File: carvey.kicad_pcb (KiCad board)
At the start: 2 copper layers, 48.2 x 14.7 mm, 6 parts, among them J1 Conn_01x04, SW1 SW_Push_Dual

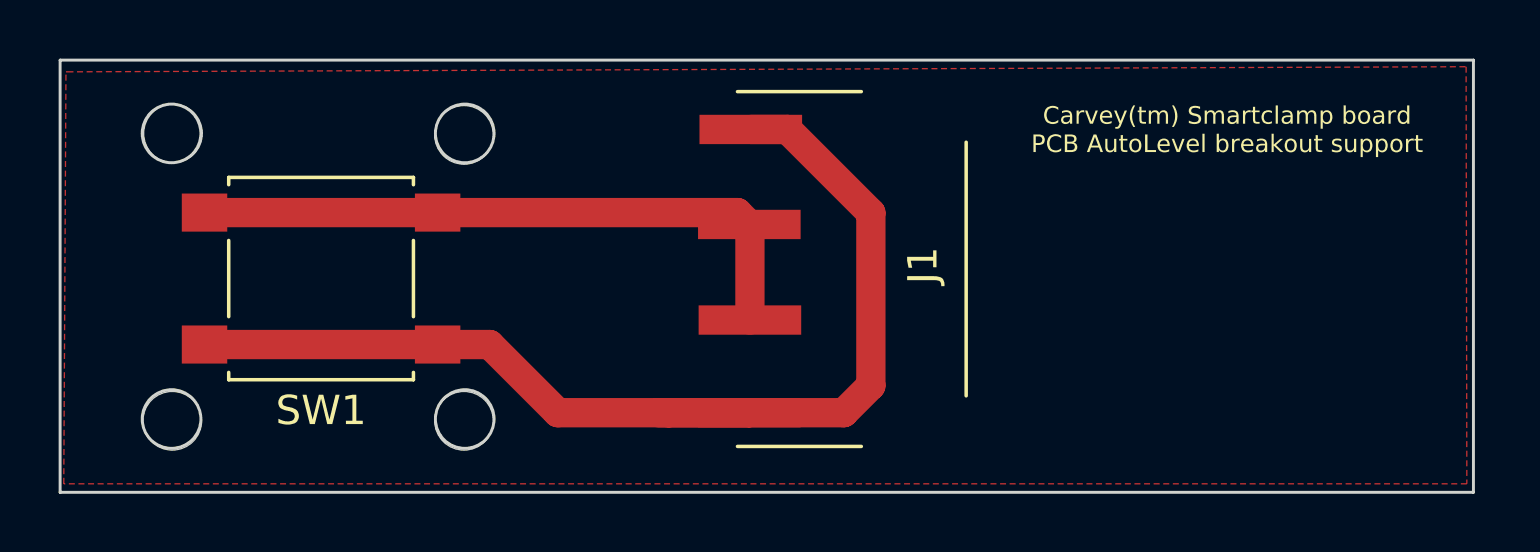
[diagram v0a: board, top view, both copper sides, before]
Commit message: Plain board to be cut out from the copper clad
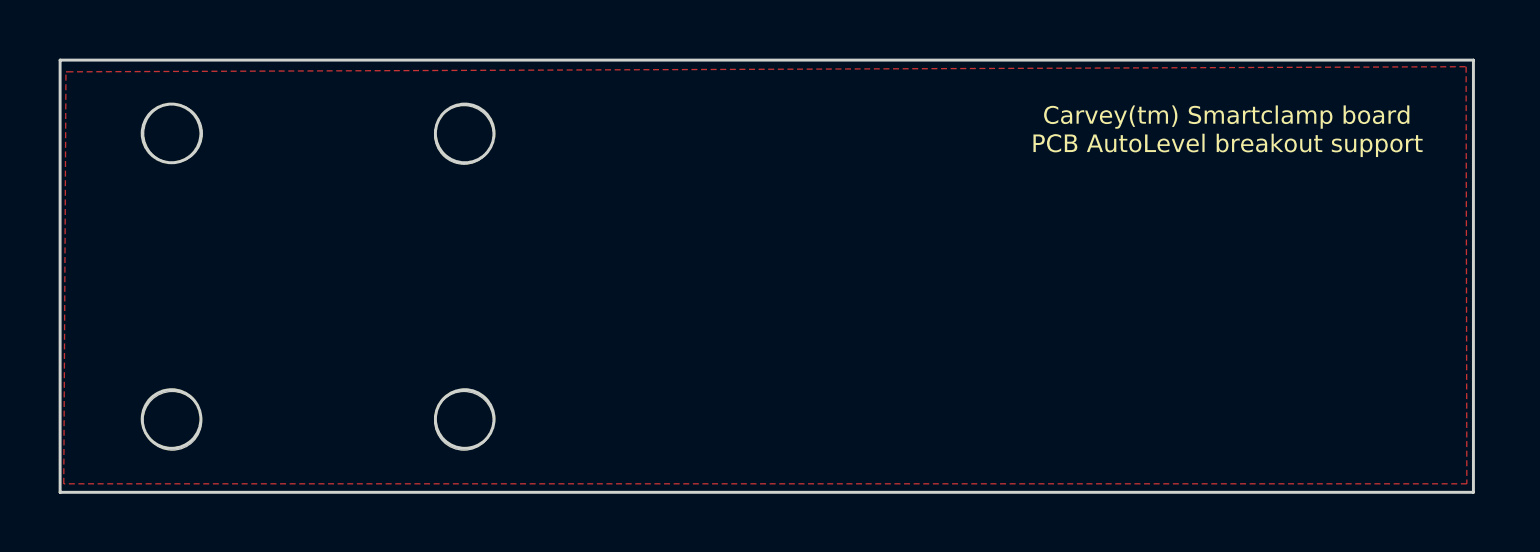
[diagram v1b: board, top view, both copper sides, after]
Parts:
- removed J1: Conn_01x04, KiCad/Connectors_JST.pretty:JST_PH_S4B-PH-SM4-TB_04x2.00mm_Angled
- removed SW1: SW_Push_Dual, KiCad/Buttons_Switches_SMD.pretty:SW_SPST_B3S-1000
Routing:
- net Net-(J1-Pad1): track 38.3 -> 0.00 mm
- net Net-(J1-Pad2): track 22.0 -> 0.00 mm
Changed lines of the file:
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@@
   (thickness 1.6)
   (drawings 10)
-  (tracks 16)
+  (tracks 0)
   (zones 0)
-  (modules 6)
-  (nets 3)
+  (modules 4)
+  (nets 1)
 )
 (page A4)
@@
   (thickness 1.6)
   (drawings 10)
-  (tracks 16)
+  (tracks 0)
   (zones 0)
-  (modules 6)
-  (nets 3)
+  (modules 4)
+  (nets 1)
 )
 (page A4)
@@
 )
 (net 0 "")
-(net 1 "Net-(J1-Pad1)")
-(net 2 "Net-(J1-Pad2)")
 (net_class Default "This is the default net class."
   (clearance 0.2)
@@
   (uvia_dia 0.3)
   (uvia_drill 0.1)
-  (add_net "Net-(J1-Pad1)")
-  (add_net "Net-(J1-Pad2)")
 )
   (module adamgreig/agg-kicad/agg.pretty:M2.5_HOLE (layer F.Cu)
@@
     (pad "" np_thru_hole circle (at 0 0) (size 2 2) (drill 2) (layers *.Cu F.Mask))
   )
-  (module KiCad/Connectors_JST.pretty:JST_PH_S4B-PH-SM4-TB_04x2.00mm_Angled (layer F.Cu)
-    (at 153.5 95.025 90)
-    (descr "JST PH series connector, S4B-PH-SM4-TB, side entry type, surface mount, Datasheet: http://www.jst-mfg.com/product/pdf/eng/ePH.pdf")
-    (tags "connector jst ph")
-    (attr smd)
-    (fp_text reference J1 (at 0.125 3 90) (layer F.SilkS)
-      (effects (font (size 1 1) (thickness 0.15)))
-    )
-    (fp_text value Conn_01x04 (at 0 5.375 90) (layer F.Fab)
-      (effects (font (size 1 1) (thickness 0.15)))
-    )
-    (fp_line (start -5.95 -3.225) (end -5.95 4.375) (layer F.Fab) (width 0.1))
-    (fp_line (start -5.95 4.375) (end 5.95 4.375) (layer F.Fab) (width 0.1))
-    (fp_line (start 5.95 4.375) (end 5.95 -3.225) (layer F.Fab) (width 0.1))
-    (fp_line (start -6.05 -3.325) (end -6.05 0.9) (layer F.SilkS) (width 0.12))
-    (fp_line (start 6.05 0.9) (end 6.05 -3.325) (layer F.SilkS) (width 0.12))
-    (fp_line (start -4.325 4.475) (end 4.325 4.475) (layer F.SilkS) (width 0.12))
-    (fp_line (start -6.6 -5.13) (end -6.6 5.07) (layer F.CrtYd) (width 0.05))
-    (fp_line (start -6.6 5.07) (end 6.6 5.07) (layer F.CrtYd) (width 0.05))
-    (fp_line (start 6.6 5.07) (end 6.6 -5.13) (layer F.CrtYd) (width 0.05))
-    (fp_line (start 6.6 -5.13) (end -6.6 -5.13) (layer F.CrtYd) (width 0.05))
-    (fp_text user %R (at 0 1.5 90) (layer F.Fab)
-      (effects (font (size 1 1) (thickness 0.15)))
-    )
-    (pad 1 smd rect (at -4.9 -2.92 90) (size 1 3.5) (layers F.Cu F.Paste F.Mask)
-      (net 1 "Net-(J1-Pad1)"))
-    (pad 2 smd rect (at -1.74 -2.9 90) (size 1 3.5) (layers F.Cu F.Paste F.Mask)
-      (net 2 "Net-(J1-Pad2)"))
-    (pad 3 smd rect (at 1.52 -2.92 90) (size 1 3.5) (layers F.Cu F.Paste F.Mask)
-      (net 2 "Net-(J1-Pad2)"))
-    (pad 4 smd rect (at 4.76 -2.87 90) (size 1 3.5) (layers F.Cu F.Paste F.Mask)
-      (net 1 "Net-(J1-Pad1)"))
-    (model ${KISYS3DMOD}/Connectors_JST.3dshapes/JST_PH_S4B-PH-SM4-TB_04x2.00mm_Angled.wrl
-      (at (xyz 0 0 0))
-      (scale (xyz 1 1 1))
-      (rotate (xyz 0 0 0))
-    )
-  )
-  (module KiCad/Buttons_Switches_SMD.pretty:SW_SPST_B3S-1000 (layer F.Cu)
-    (at 135.975 95.35 180)
-    (descr "Surface Mount Tactile Switch for High-Density Packaging")
-    (tags "Tactile Switch")
-    (attr smd)
-    (fp_text reference SW1 (at 0 -4.5 180) (layer F.SilkS)
-      (effects (font (size 1 1) (thickness 0.15)))
-    )
-    (fp_text value SW_Push_Dual (at 0 4.5 180) (layer F.Fab)
-      (effects (font (size 1 1) (thickness 0.15)))
-    )
-    (fp_text user %R (at 0 -4.5 180) (layer F.Fab)
-      (effects (font (size 1 1) (thickness 0.15)))
-    )
-    (fp_line (start -5 3.7) (end 5 3.7) (layer F.CrtYd) (width 0.05))
-    (fp_line (start 5 3.7) (end 5 -3.7) (layer F.CrtYd) (width 0.05))
-    (fp_line (start 5 -3.7) (end -5 -3.7) (layer F.CrtYd) (width 0.05))
-    (fp_line (start -5 -3.7) (end -5 3.7) (layer F.CrtYd) (width 0.05))
-    (fp_line (start -3.15 -3.2) (end -3.15 -3.45) (layer F.SilkS) (width 0.12))
-    (fp_line (start -3.15 -3.45) (end 3.15 -3.45) (layer F.SilkS) (width 0.12))
-    (fp_line (start 3.15 -3.45) (end 3.15 -3.2) (layer F.SilkS) (width 0.12))
-    (fp_line (start -3.15 1.3) (end -3.15 -1.3) (layer F.SilkS) (width 0.12))
-    (fp_line (start 3.15 3.2) (end 3.15 3.45) (layer F.SilkS) (width 0.12))
-    (fp_line (start 3.15 3.45) (end -3.15 3.45) (layer F.SilkS) (width 0.12))
-    (fp_line (start -3.15 3.45) (end -3.15 3.2) (layer F.SilkS) (width 0.12))
-    (fp_line (start 3.15 -1.3) (end 3.15 1.3) (layer F.SilkS) (width 0.12))
-    (fp_circle (center 0 0) (end 1.65 0) (layer F.Fab) (width 0.1))
-    (fp_line (start -3 -3.3) (end 3 -3.3) (layer F.Fab) (width 0.1))
-    (fp_line (start 3 -3.3) (end 3 3.3) (layer F.Fab) (width 0.1))
-    (fp_line (start 3 3.3) (end -3 3.3) (layer F.Fab) (width 0.1))
-    (fp_line (start -3 3.3) (end -3 -3.3) (layer F.Fab) (width 0.1))
-    (pad 1 smd rect (at -3.975 -2.25 180) (size 1.55 1.3) (layers F.Cu F.Paste F.Mask)
-      (net 1 "Net-(J1-Pad1)"))
-    (pad 1 smd rect (at 3.975 -2.25 180) (size 1.55 1.3) (layers F.Cu F.Paste F.Mask)
-      (net 1 "Net-(J1-Pad1)"))
-    (pad 2 smd rect (at -3.975 2.25 180) (size 1.55 1.3) (layers F.Cu F.Paste F.Mask)
-      (net 2 "Net-(J1-Pad2)"))
-    (pad 2 smd rect (at 3.975 2.25 180) (size 1.55 1.3) (layers F.Cu F.Paste F.Mask)
-      (net 2 "Net-(J1-Pad2)"))
-    (model ${KISYS3DMOD}/Buttons_Switches_SMD.3dshapes/SW_SPST_B3S-1000.wrl
-      (at (xyz 0 0 0))
-      (scale (xyz 1 1 1))
-      (rotate (xyz 0 0 0))
-    )
-  )
   (target plus (at 126.875 102.65) (size 5) (width 0.15) (layer Edge.Cuts))
   (gr_text "Carvey(tm) Smartclamp board\nPCB AutoLevel breakout support" (at 166.875 90.275) (layer F.SilkS)
@@
   (gr_line (start 175.275 87.9) (end 175.275 102.64) (layer Edge.Cuts) (width 0.1))
   (gr_circle (center 130.875 90.4) (end 131.875 90.4) (layer Edge.Cuts) (width 0.1))
-  (segment (start 132 97.6) (end 139.95 97.6) (width 1) (layer F.Cu) (net 1))
-  (segment (start 139.95 97.6) (end 141.725 97.6) (width 1) (layer F.Cu) (net 1))
-  (segment (start 141.725 97.6) (end 144.05 99.925) (width 1) (layer F.Cu) (net 1))
-  (segment (start 144.05 99.925) (end 147.83 99.925) (width 1) (layer F.Cu) (net 1))
-  (segment (start 147.83 99.925) (end 150.58 99.925) (width 1) (layer F.Cu) (net 1))
-  (segment (start 147.475 99.925) (end 150.58 99.925) (width 1) (layer F.Cu) (net 1))
-  (segment (start 154.725 99) (end 153.8 99.925) (width 1) (layer F.Cu) (net 1))
-  (segment (start 153.8 99.925) (end 150.58 99.925) (width 1) (layer F.Cu) (net 1))
-  (segment (start 154.725 93.11) (end 154.725 99) (width 1) (layer F.Cu) (net 1))
-  (segment (start 150.63 90.265) (end 151.88 90.265) (width 1) (layer F.Cu) (net 1))
-  (segment (start 151.88 90.265) (end 154.725 93.11) (width 1) (layer F.Cu) (net 1))
-  (segment (start 139.95 93.1) (end 150.175 93.1) (width 1) (layer F.Cu) (net 2))
-  (segment (start 150.175 93.1) (end 150.58 93.505) (width 1) (layer F.Cu) (net 2))
-  (segment (start 132 93.1) (end 139.95 93.1) (width 1) (layer F.Cu) (net 2))
-  (segment (start 150.6 96.765) (end 150.6 93.525) (width 1) (layer F.Cu) (net 2))
-  (segment (start 150.6 93.525) (end 150.58 93.505) (width 1) (layer F.Cu) (net 2))
   (zone (net 0) (net_name "") (layer F.Cu) (hatch edge 0.508)
     (connect_pads (clearance 0.508))
